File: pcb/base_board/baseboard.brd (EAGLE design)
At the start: 88 x 85 mm, 38 parts, among them IC1 LD117AS33TR, SW1 324_SW, SW2 324_SW, SW20 324_SW, SW3 324_SW, SW4 324_SW, U5 CH340C

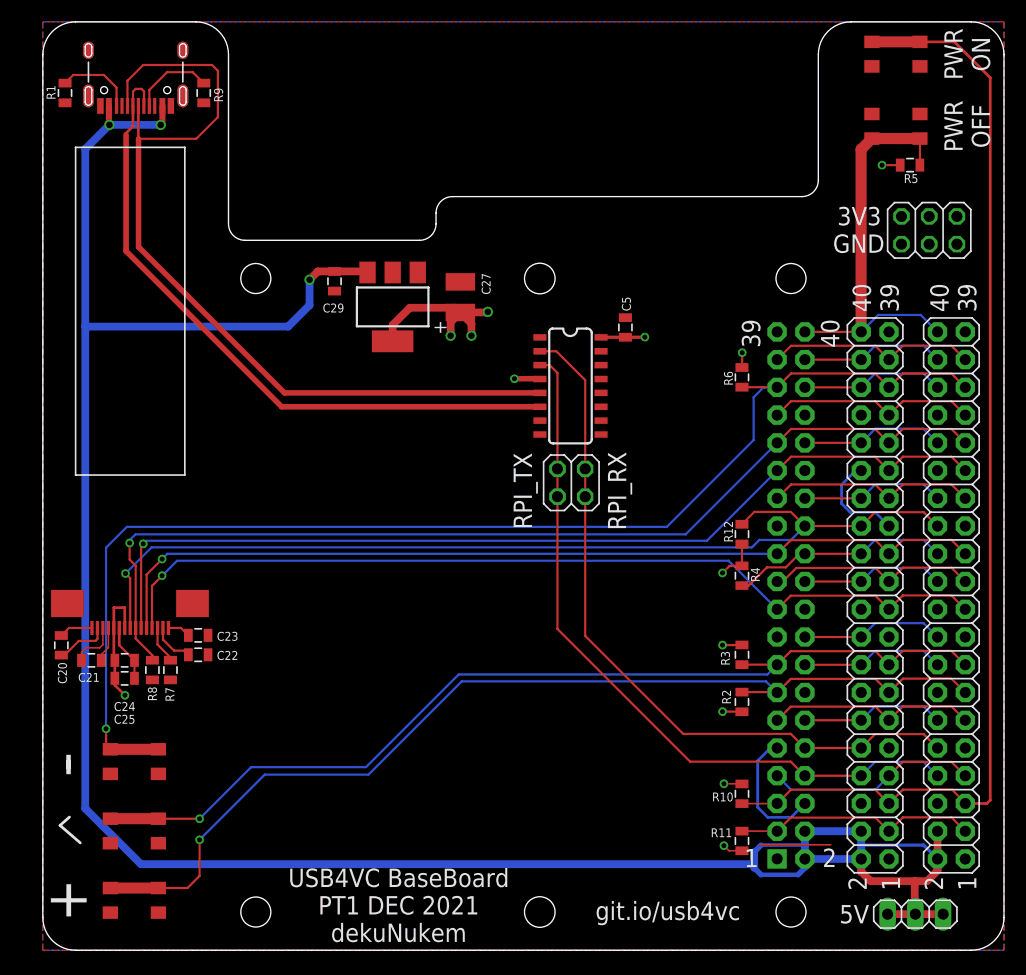
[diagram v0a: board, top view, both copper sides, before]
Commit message: added standoff information, updated silkscreen for next prototype
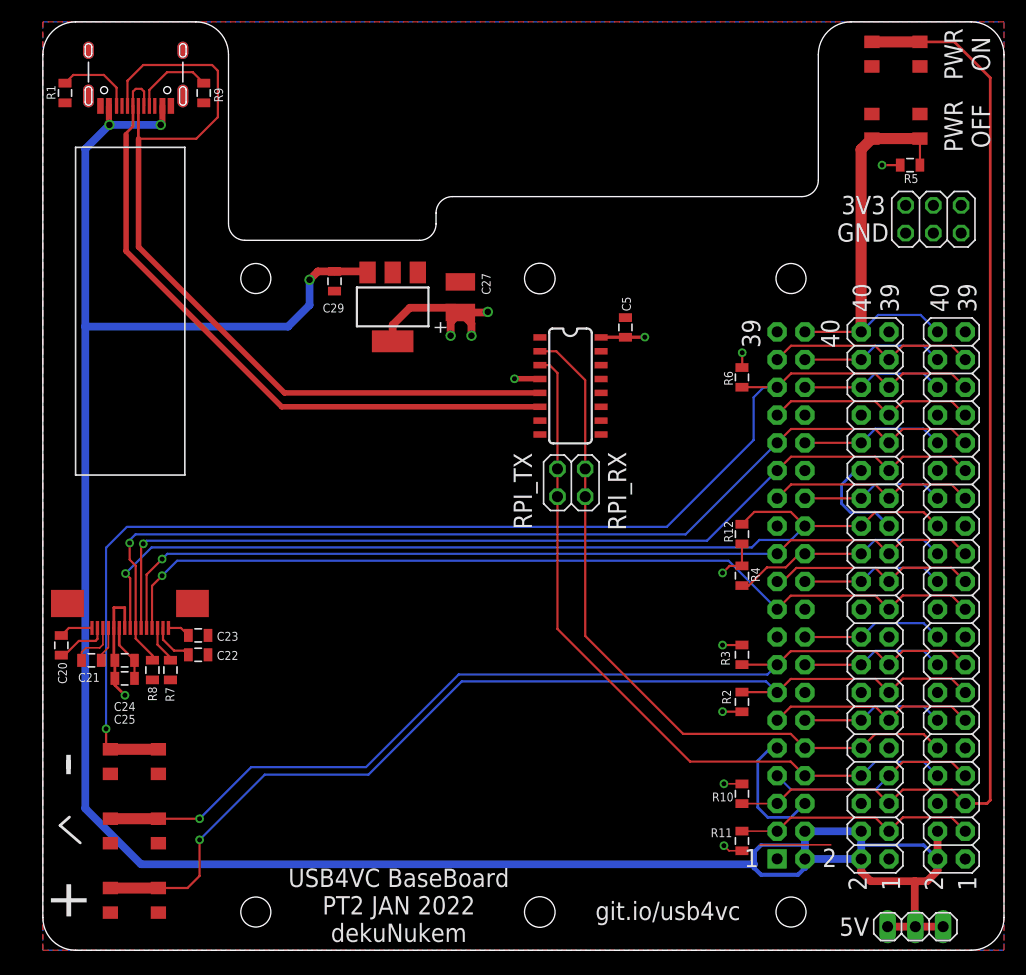
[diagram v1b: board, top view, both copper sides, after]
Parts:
- moved JP5 1.14 mm to (79.9, 2.16)
- moved JP6 1.09 mm to (81.5, 66.9)
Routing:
- net +5V: track 220.3 -> 221.5 mm
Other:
- board text added: "USB4VC BaseBoard PT2 JAN 2022 dekuNukem"
- board text removed: "USB4VC BaseBoard PT1 DEC 2021 dekuNukem"
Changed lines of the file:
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@@
 <circle x="19.5" y="61.5" radius="3" width="0" layer="42"/>
 <text x="32.5882" y="4.1148" size="1.6764" layer="25" rot="R180" align="center">USB4VC BaseBoard
-PT1 DEC 2021
+PT2 JAN 2022
 dekuNukem</text>
-<text x="74.7522" y="67.2084" size="1.6764" layer="25" rot="R180" align="center">3V3</text>
-<text x="74.7014" y="64.6938" size="1.6764" layer="25" rot="R180" align="center">GND</text>
-<text x="72.9234" y="2.4638" size="1.6764" layer="25">5V</text>
+<text x="75.1332" y="68.2244" size="1.6764" layer="25" rot="R180" align="center">3V3</text>
+<text x="75.0824" y="65.7098" size="1.6764" layer="25" rot="R180" align="center">GND</text>
+<text x="72.9234" y="1.3208" size="1.6764" layer="25">5V</text>
 <text x="85.471" y="5.461" size="1.6764" layer="25" rot="R90">1</text>
 <text x="82.423" y="5.461" size="1.6764" layer="25" rot="R90">2</text>
@@
 <attribute name="NAME" x="62.9031" y="26.0604" size="0.8128" layer="25" rot="R90"/>
 </element>
-<element name="JP5" library="pinhead" library_urn="urn:adsk.eagle:library:325" package="1X03" package3d_urn="urn:adsk.eagle:package:22458/2" value="" x="79.883" y="3.302" smashed="yes">
-<attribute name="POPULARITY" value="92" x="79.883" y="3.302" size="0.8128" layer="27" display="off"/>
-<attribute name="VALUE" x="76.073" y="0.127" size="1.27" layer="27"/>
+<element name="JP5" library="pinhead" library_urn="urn:adsk.eagle:library:325" package="1X03" package3d_urn="urn:adsk.eagle:package:22458/2" value="" x="79.883" y="2.159" smashed="yes">
+<attribute name="POPULARITY" value="92" x="79.883" y="2.159" size="0.8128" layer="27" display="off"/>
+<attribute name="VALUE" x="76.073" y="-1.016" size="1.27" layer="27"/>
 </element>
 <element name="SW2" library="3pos_slide_switch_centered" package="342_SWICH_FOOT" value="324_SW" x="78.105" y="82.042" smashed="yes"/>
@@
 <attribute name="NAME" x="63.1825" y="37.338" size="0.8128" layer="25" rot="R90"/>
 </element>
-<element name="JP6" library="pinhead" library_urn="urn:adsk.eagle:library:325" package="2X03" package3d_urn="urn:adsk.eagle:package:22462/2" value="" x="81.153" y="65.913" smashed="yes">
-<attribute name="POPULARITY" value="62" x="81.153" y="65.913" size="1.778" layer="27" display="off"/>
-<attribute name="VALUE" x="77.343" y="61.468" size="1.27" layer="27"/>
+<element name="JP6" library="pinhead" library_urn="urn:adsk.eagle:library:325" package="2X03" package3d_urn="urn:adsk.eagle:package:22462/2" value="" x="81.534" y="66.929" smashed="yes">
+<attribute name="POPULARITY" value="62" x="81.534" y="66.929" size="1.778" layer="27" display="off"/>
+<attribute name="VALUE" x="77.724" y="62.484" size="1.27" layer="27"/>
 </element>
 </elements>
@@
 <contactref element="PCB1" pad="P$2"/>
 <contactref element="PCB1" pad="P$4"/>
-<wire x1="65.1256" y1="7.5438" x2="65.7606" y2="6.9088" width="0.508" layer="16"/>
+<wire x1="65.1256" y1="7.5438" x2="65.7606" y2="6.9088" width="0.381" layer="16"/>
 <wire x1="69.7718" y1="7.5418" x2="69.7718" y2="8.3566" width="0.6096" layer="16"/>
-<wire x1="65.7606" y1="6.9088" x2="69.1388" y2="6.9088" width="0.4064" layer="16"/>
-<wire x1="69.1388" y1="6.9088" x2="69.7718" y2="7.5418" width="0.508" layer="16"/>
-<wire x1="65.7606" y1="9.6266" x2="65.1256" y2="8.9916" width="0.508" layer="16"/>
-<wire x1="65.1256" y1="8.9916" x2="65.1256" y2="7.874" width="0.7112" layer="16"/>
-<wire x1="65.1256" y1="7.874" x2="65.1256" y2="7.5438" width="0.7112" layer="16"/>
+<wire x1="65.7606" y1="6.9088" x2="69.1388" y2="6.9088" width="0.381" layer="16"/>
+<wire x1="69.1388" y1="6.9088" x2="69.7718" y2="7.5418" width="0.381" layer="16"/>
+<wire x1="65.7606" y1="9.6266" x2="65.1256" y2="8.9916" width="0.381" layer="16"/>
+<wire x1="65.1256" y1="8.9916" x2="65.1256" y2="7.874" width="0.508" layer="16"/>
+<wire x1="65.1256" y1="7.874" x2="65.1256" y2="7.5438" width="0.508" layer="16"/>
 <wire x1="69.7718" y1="8.3566" x2="69.7718" y2="9.6266" width="0.7112" layer="16"/>
 <wire x1="69.7718" y1="9.6266" x2="69.7718" y2="10.8966" width="0.7112" layer="16"/>
@@
 <contactref element="JP2" pad="2"/>
 <contactref element="JP2" pad="4"/>
-<wire x1="65.7606" y1="9.6266" x2="69.7718" y2="9.6266" width="0.3302" layer="16"/>
+<wire x1="65.7606" y1="9.6266" x2="69.7718" y2="9.6266" width="0.3048" layer="16"/>
 <wire x1="6.096" y1="75.565" x2="3.8862" y2="73.3552" width="0.7112" layer="16"/>
 <wire x1="8.9916" y1="7.874" x2="65.1256" y2="7.874" width="0.7112" layer="16"/>
@@
 <contactref element="JP5" pad="2"/>
 <contactref element="JP5" pad="3"/>
-<wire x1="79.8322" y1="6.3246" x2="79.8322" y2="3.3528" width="0.7112" layer="1"/>
-<wire x1="79.8322" y1="3.3528" x2="79.883" y2="3.302" width="0.7112" layer="1"/>
-<wire x1="77.343" y1="3.302" x2="79.7814" y2="3.302" width="0.7112" layer="1"/>
-<wire x1="79.7814" y1="3.302" x2="79.8322" y2="3.3528" width="0.7112" layer="1"/>
-<wire x1="79.883" y1="3.302" x2="82.423" y2="3.302" width="0.7112" layer="1"/>
+<wire x1="79.8322" y1="6.3246" x2="79.8322" y2="2.2098" width="0.7112" layer="1"/>
+<wire x1="79.8322" y1="2.2098" x2="79.883" y2="2.159" width="0.7112" layer="1"/>
+<wire x1="77.343" y1="2.159" x2="79.7814" y2="2.159" width="0.7112" layer="1"/>
+<wire x1="79.7814" y1="2.159" x2="79.8322" y2="2.2098" width="0.7112" layer="1"/>
+<wire x1="79.883" y1="2.159" x2="82.423" y2="2.159" width="0.7112" layer="1"/>
 <wire x1="69.7718" y1="10.8966" x2="74.93" y2="10.8966" width="0.7112" layer="16"/>
 <wire x1="3.8862" y1="73.3552" x2="3.8862" y2="57.0992" width="0.7112" layer="16"/>
